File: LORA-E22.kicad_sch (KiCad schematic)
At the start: 16 parts, among them J5 Conn_Coaxial, U3 E22P-915M30S

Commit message: next revision pcb progress
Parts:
- removed C12: 100nF, Capacitor_SMD:C_0402_1005Metric, symbol Device:C_Small
- removed C15: 10uF, Capacitor_SMD:C_0402_1005Metric, symbol Device:C_Small
- removed C18: 47uF, Capacitor_SMD:C_0805_2012Metric, symbol Device:C_Small
- removed C26: 680uF, Capacitor_SMD:CP_Elec_8x10, symbol Device:C_Polarized
- removed D6: SMAJ3.3A, Diode_SMD:D_SMA-SMB_Universal_Handsoldering, symbol Diode:SMAJ5.0A
- removed D8: BESDU0603-14, Diode_SMD:D_0603_1608Metric, symbol Device:D_TVS
- removed R29: 0, Resistor_SMD:R_0402_1005Metric, symbol Device:R_Small
- added C12, C15, C18, C29: 100uF, Capacitor_SMD:C_1210_3225Metric, symbol Device:C
- added C26: 10uF, Capacitor_SMD:C_0402_1005Metric, symbol Device:C_Small
- added C36: 47pF C0G/NP0, Capacitor_SMD:C_0402_1005Metric, symbol Device:C_Small
- added C37, C38: 10nF, Capacitor_SMD:C_0402_1005Metric_Pad0.74x0.62mm_HandSolder, symbol Device:C_Small
- added D7: PGB1010603, Capacitor_SMD:C_0603_1608Metric, symbol Device:D_TVS
- added FL2: 0900LP15B0063001E, easyeda2kicad:FILTER-SMD_0805-8P-L2.0-W1.2-TL, symbol easyeda2kicad:0900LP15B0063001E
- added JP6: BYPASS_FILTER, Jumper:SolderJumper-2_P1.3mm_Open_RoundedPad1.0x1.5mm, symbol Jumper:Jumper_2_Open
- added R37: 0, Resistor_SMD:R_0402_1005Metric_Pad0.72x0.64mm_HandSolder, symbol Device:R
- added U5: TPS259571DSGR, easyeda2kicad:WSON-8_L2.0-W2.0-P0.50-TL-EP, symbol easyeda2kicad:TPS259571DSGR
- C13: value 10uF -> 100nF; Voltage Rating (none) -> 16v
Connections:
- net PRE_LORA_ANT is gone; now on net LORA_ANT: U3.21 (ANT)
- net +5V: now also C12.1, C15.1, C18.1, C26.1, C29.1
- net GND: now also C12.2, C15.2, C18.2, C26.2, C29.2, C37.2, C38.2, D7.1 (A1), FL2.1 (GND), FL2.3 (GND), FL2.5 (GND), FL2.7 (GND)
- net LORA_ANT: now also C36.1; no longer J5.1 (In)
- new net: C38.1, FL2.4 (IO), JP6.1 (A), R37.2
- new net: C36.2, FL2.8 (IO), JP6.2 (B)
- new net: C37.1, D7.2 (A2), J5.1 (In), R37.1
- no-connect marks 0 -> 2
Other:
- note added: "900MHz Wide Band Low Pass Filter"
- note added: "DC Block"
- note added: "Optional Matching"
- note added: "SMA Connector"
- note removed: "BESDU0603 working voltage >= 12v"
- note removed: "Optional polymer capacitor for extra stability"
- moved on the sheet: C11, R15

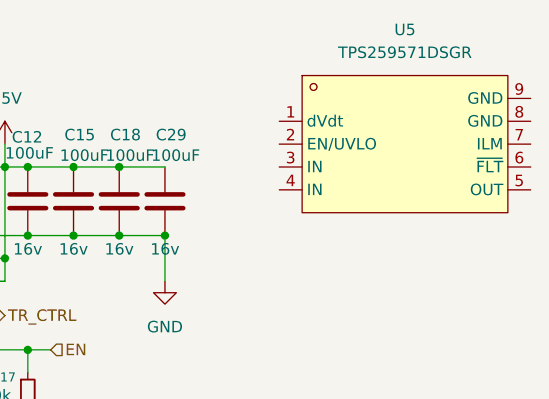
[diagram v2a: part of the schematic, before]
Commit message: update schematic with new eFuse and add journal.md
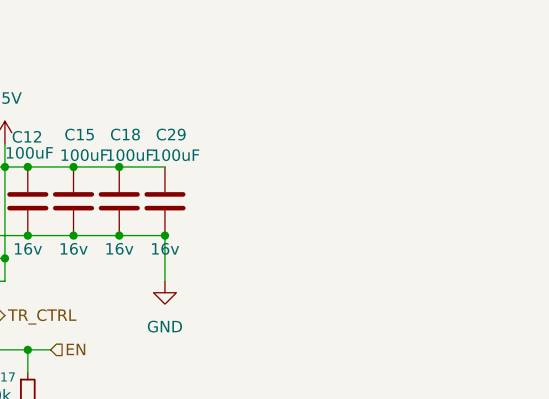
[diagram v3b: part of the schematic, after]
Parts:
- removed U5: TPS259571DSGR, easyeda2kicad:WSON-8_L2.0-W2.0-P0.50-TL-EP, symbol easyeda2kicad:TPS259571DSGR
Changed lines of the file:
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@@
-	)
-	(symbol
-		(lib_id "easyeda2kicad:TPS259571DSGR")
-		(at 240.03 71.12 0)
-		(unit 1)
-		(body_style 1)
-		(exclude_from_sim no)
-		(in_bom yes)
-		(on_board yes)
-		(in_pos_files yes)
-		(dnp no)
-		(fields_autoplaced yes)
-		(property "Reference" "U5"
-			(at 240.03 58.42 0)
-			(show_name no)
-			(do_not_autoplace no)
-			(effects
-				(font
-					(size 1.27 1.27)
-				)
-			)
-		)
-		(property "Value" "TPS259571DSGR"
-			(at 240.03 60.96 0)
-			(show_name no)
-			(do_not_autoplace no)
-			(effects
-				(font
-					(size 1.27 1.27)
-				)
-			)
-		)
-		(property "Footprint" "easyeda2kicad:WSON-8_L2.0-W2.0-P0.50-TL-EP"
-			(at 240.03 83.82 0)
-			(hide yes)
-			(show_name no)
-			(do_not_autoplace no)
-			(effects
-				(font
-					(size 1.27 1.27)
-				)
-			)
-		)
-		(property "Datasheet" "https://lcsc.com/product-detail/PMIC-Current-Power-Monitors-Regulators_Texas-Instruments-Texas-Instruments-TPS259571DSGR_C471038.html"
-			(at 240.03 86.36 0)
-			(hide yes)
-			(show_name no)
-			(do_not_autoplace no)
-			(effects
-				(font
-					(size 1.27 1.27)
-				)
-			)
-		)
-		(property "Description" ""
-			(at 240.03 71.12 0)
-			(hide yes)
-			(show_name no)
-			(do_not_autoplace no)
-			(effects
-				(font
-					(size 1.27 1.27)
-				)
-			)
-		)
-		(property "Manufacturer" "TI(德州仪器)"
-			(at 240.03 88.9 0)
-			(hide yes)
-			(show_name no)
-			(do_not_autoplace no)
-			(effects
-				(font
-					(size 1.27 1.27)
-				)
-			)
-		)
-		(property "MPN" "TPS259571DSGR"
-			(at 240.03 91.44 0)
-			(hide yes)
-			(show_name no)
-			(do_not_autoplace no)
-			(effects
-				(font
-					(size 1.27 1.27)
-				)
-			)
-		)
-		(property "LCSC Part" "C471038"
-			(at 240.03 93.98 0)
-			(hide yes)
-			(show_name no)
-			(do_not_autoplace no)
-			(effects
-				(font
-					(size 1.27 1.27)
-				)
-			)
-		)
-		(pin "3"
-		)
-		(pin "8"
-		)
-		(pin "2"
-		)
-		(pin "5"
-		)
-		(pin "6"
-		)
-		(pin "1"
-		)
-		(pin "9"
-		)
-		(pin "7"
-		)
-		(pin "4"
-		)
-		(instances
-			(project "meshtastic"
-				(path "/fe9d4a31-2311-442f-997c-52ad8ca5cfe9/a8463f07-c31a-442f-966c-3f51ff19a9b1"
-					(reference "U5")
-					(unit 1)
-				)
-			)
-		)
 	)
 	(symbol

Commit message: revise efuse, add bat
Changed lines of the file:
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@@
-	)
-	(junction
-		(at 134.62 76.2)
-		(diameter 0)
-		(color 0 0 0 0)
 	)
 	(junction
@@
 	)
 	(junction
-		(at 134.62 95.25)
-		(diameter 0)
-		(color 0 0 0 0)
-	)
-	(junction
 		(at 208.28 81.28)
 		(diameter 0)
@@
 	(wire
 		(pts
-			(xy 120.65 86.36) (xy 120.65 95.25)
-		)
-		(stroke
-			(width 0)
-			(type default)
-		)
-	)
-	(wire
-		(pts
 			(xy 154.94 91.44) (xy 156.21 91.44)
 		)
@@
 	(wire
 		(pts
-			(xy 134.62 95.25) (xy 134.62 93.98)
-		)
-		(stroke
-			(width 0)
-			(type default)
-		)
-	)
-	(wire
-		(pts
 			(xy 203.2 81.28) (xy 208.28 81.28)
 		)
@@
 	(wire
 		(pts
-			(xy 134.62 96.52) (xy 134.62 95.25)
+			(xy 134.62 93.98) (xy 134.62 96.52)
 		)
 		(stroke
@@
 	(wire
 		(pts
-			(xy 120.65 76.2) (xy 134.62 76.2)
-		)
-		(stroke
-			(width 0)
-			(type default)
-		)
-	)
-	(wire
-		(pts
 			(xy 184.15 83.82) (xy 195.58 83.82)
 		)
@@
 	(wire
 		(pts
-			(xy 120.65 78.74) (xy 120.65 76.2)
-		)
-		(stroke
-			(width 0)
-			(type default)
-		)
-	)
-	(wire
-		(pts
 			(xy 185.42 74.93) (xy 185.42 73.66)
 		)
@@
 		)
 		(stroke
-			(width 0)
-			(type default)
-		)
-	)
-	(wire
-		(pts
-			(xy 120.65 95.25) (xy 134.62 95.25)
-		)
-		(stroke

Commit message: add BMS and charge controller!
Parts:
- added D9: ESD9B5.0ST5G, Diode_SMD:D_SOD-923, symbol Diode:ESD9B5.0ST5G
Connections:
- net +5V: now also D9.2 (A2)
- net GND: now also D9.1 (A1)
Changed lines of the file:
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@@
+	)
+	(junction
+		(at 213.36 73.66)
+		(diameter 0)
+		(color 0 0 0 0)
 	)
 	(junction
@@
 	(wire
 		(pts
+			(xy 213.36 81.28) (xy 219.71 81.28)
+		)
+		(stroke
+			(width 0)
+			(type default)
+		)
+	)
+	(wire
+		(pts
 			(xy 67.31 165.1) (xy 67.31 167.64)
 		)
@@
 		(pts
 			(xy 76.2 165.1) (xy 82.55 165.1)
+		)
+		(stroke
+			(width 0)
+			(type default)
+		)
+	)
+	(wire
+		(pts
+			(xy 213.36 73.66) (xy 219.71 73.66)
 		)
 		(stroke
@@
 					(unit 1)
 				)
+			)
+		)
+	)
+	(symbol
+		(lib_id "Diode:ESD9B5.0ST5G")
+		(at 219.71 77.47 90)
+		(unit 1)
+		(body_style 1)
+		(exclude_from_sim no)
+		(in_bom yes)
+		(on_board yes)
+		(in_pos_files yes)
+		(dnp no)
+		(fields_autoplaced yes)
+		(property "Reference" "D9"
+			(at 222.25 76.1999 90)
+			(show_name no)
+			(do_not_autoplace no)
+			(effects
+				(font
+					(size 1.27 1.27)
+				)
+				(justify right)
+			)
+		)
+		(property "Value" "ESD9B5.0ST5G"
+			(at 222.25 78.7399 90)
+			(show_name no)
+			(do_not_autoplace no)
+			(effects
+				(font
+					(size 1.27 1.27)
+				)
+				(justify right)
+			)
+		)
+		(property "Footprint" "Diode_SMD:D_SOD-923"
+			(at 219.71 77.47 0)
+			(hide yes)
+			(show_name no)
+			(do_not_autoplace no)
+			(effects
+				(font
+					(size 1.27 1.27)
+				)
+			)
+		)
+		(property "Datasheet" "https://www.onsemi.com/pub/Collateral/ESD9B-D.PDF"
+			(at 219.71 77.47 0)
+			(hide yes)
+			(show_name no)
+			(do_not_autoplace no)
+			(effects
+				(font
+					(size 1.27 1.27)
+				)
+			)
+		)
+		(property "Description" "ESD protection diode, 5.0Vrwm, SOD-923"
+			(at 219.71 77.47 0)
+			(hide yes)
+			(show_name no)
+			(do_not_autoplace no)
+			(effects
+				(font
+					(size 1.27 1.27)
+				)
+			)
+		)
+		(pin "2"
+		)
+		(pin "1"
+		)
+		(instances
+			(project "meshtastic"
+				(path "/fe9d4a31-2311-442f-997c-52ad8ca5cfe9/a8463f07-c31a-442f-966c-3f51ff19a9b1"
+					(reference "D9")
+					(unit 1)
+				)

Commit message: update bms schematic, minor changes to rest
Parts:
- C37, C38: value 10nF -> 1pF C0G
- JP6: footprint Jumper:SolderJumper-2_P1.3mm_Open_RoundedPad1.0x1.5mm -> Resistor_SMD:R_0402_1005Metric; now not fitted
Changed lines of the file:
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@@
 		(in_pos_files yes)
 		(dnp yes)
-		(fields_autoplaced yes)
 		(property "Reference" "C38"
 			(at 69.85 168.9162 0)
@@
 			)
 		)
-		(property "Value" "10nF"
-			(at 69.85 171.4562 0)
+		(property "Value" "1pF C0G"
+			(at 56.642 173.482 0)
+			(hide yes)
 			(show_name no)
 			(do_not_autoplace no)
@@
 		(in_pos_files yes)
 		(dnp yes)
-		(fields_autoplaced yes)
 		(property "Reference" "C37"
 			(at 54.61 168.9162 0)
@@
 			)
 		)
-		(property "Value" "10nF"
-			(at 54.61 171.4562 0)
+		(property "Value" "1pF C0G"
+			(at 54.61 170.942 0)
 			(show_name no)
 			(do_not_autoplace no)
@@
 		(on_board yes)
 		(in_pos_files yes)
-		(dnp no)
+		(dnp yes)
 		(property "Reference" "JP6"
 			(at 91.44 169.926 0)
@@
 			)
 		)
-		(property "Footprint" "Jumper:SolderJumper-2_P1.3mm_Open_RoundedPad1.0x1.5mm"
+		(property "Footprint" "Resistor_SMD:R_0402_1005Metric"
 			(at 91.44 172.72 0)
 			(hide yes)
